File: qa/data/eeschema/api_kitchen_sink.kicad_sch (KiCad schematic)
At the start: 1 part

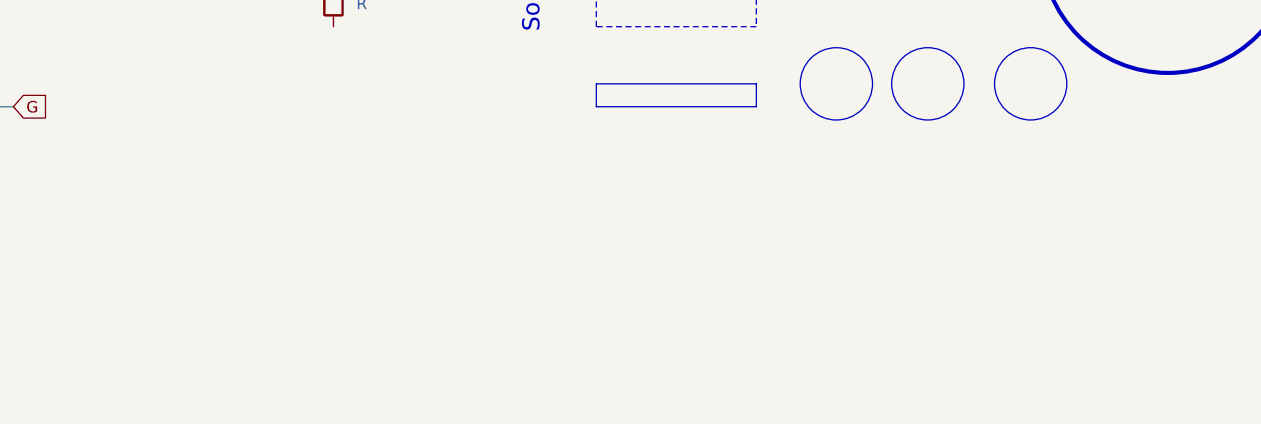
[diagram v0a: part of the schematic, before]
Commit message: API: add sch group and sheet symbol support
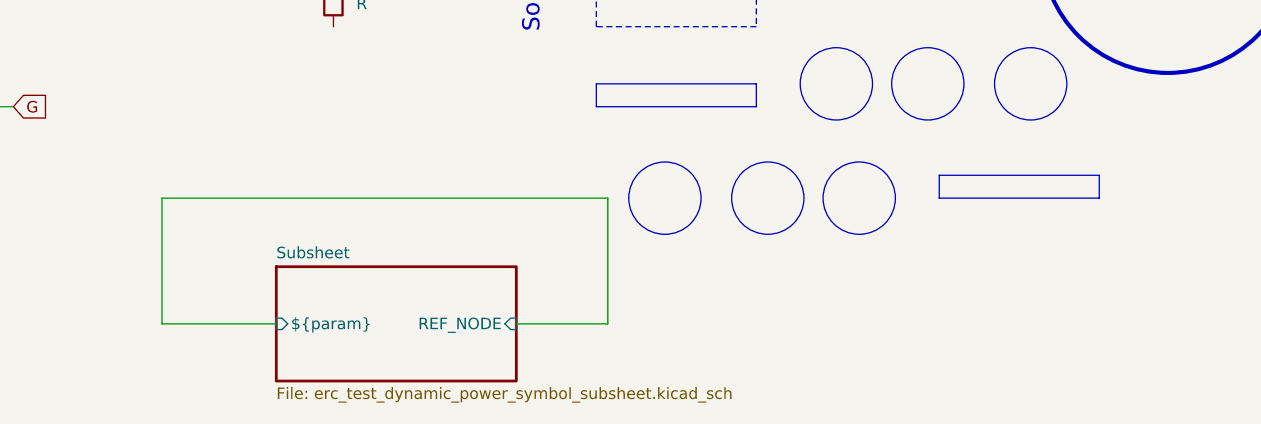
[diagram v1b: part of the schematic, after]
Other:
- added sheet Subsheet (erc_test_dynamic_power_symbol_subsheet.kicad_sch)
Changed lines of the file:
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@@
 		)
+	)
+	(circle
+		(center 157.48 63.5)
+		(radius 4.0161)
+		(stroke
+			(width 0)
+			(type solid)
+		)
+		(fill
+			(type cross_hatch)
+			(color 58 104 255 1)
+		)
+		(locked yes)
 	)
 	(bezier
@@
 	)
 	(circle
+		(center 167.64 63.5)
+		(radius 4.0161)
+		(stroke
+			(width 0)
+			(type default)
+		)
+		(fill
+			(type none)
+		)
+		(locked yes)
+	)
+	(circle
 		(center 201.93 35.56)
 		(radius 14.0276)
@@
 			(type none)
 		)
+	)
+	(circle
+		(center 146.05 63.5)
+		(radius 4.0161)
+		(stroke
+			(width 0)
+			(type solid)
+		)
+		(fill
+			(type reverse_hatch)
+			(color 0 0 0 0)
+		)
+		(locked yes)
+	)
+	(rectangle
+		(start 194.31 63.5)
+		(end 176.53 60.96)
+		(stroke
+			(width 0)
+			(type solid)
+		)
+		(fill
+			(type hatch)
+			(color 255 64 87 1)
+		)
+		(locked yes)
 	)
 	(text "Some text"
@@
 	(wire
 		(pts
+			(xy 102.87 77.47) (xy 90.17 77.47)
+		)
+		(stroke
+			(width 0)
+			(type default)
+		)
+	)
+	(wire
+		(pts
 			(xy 59.69 40.64) (xy 59.69 53.34)
 		)
@@
 	(wire
 		(pts
+			(xy 139.7 77.47) (xy 129.54 77.47)
+		)
+		(stroke
+			(width 0)
+			(type default)
+		)
+	)
+	(wire
+		(pts
 			(xy 87.63 27.94) (xy 80.01 27.94)
 		)
@@
 		(pts
 			(xy 48.26 25.4) (xy 48.26 19.05)
+		)
+		(stroke
+			(width 0)
+			(type default)
+		)
+	)
+	(wire
+		(pts
+			(xy 90.17 77.47) (xy 90.17 63.5)
 		)
 		(stroke
@@
 	(wire
 		(pts
+			(xy 139.7 63.5) (xy 139.7 77.47)
+		)
+		(stroke
+			(width 0)
+			(type default)
+		)
+	)
+	(wire
+		(pts
 			(xy 53.34 40.64) (xy 59.69 40.64)
 		)
@@
 		(pts
 			(xy 59.69 40.64) (xy 80.01 40.64)
+		)
+		(stroke
+			(width 0)
+			(type default)
+		)
+	)
+	(wire
+		(pts
+			(xy 90.17 63.5) (xy 139.7 63.5)
 		)
 		(stroke
@@
 				)
 			)
+		)
+	)
+	(group "MyGroup"
+		(locked yes)
+		(members "1c20a5ba-7190-401a-b021-abb688d52ffd" "bf6e7e59-beed-4ba7-a7bf-ffa7476e6e5d"
+			"e335506b-7a34-4e1e-bd33-077d7ea2b1b5" "e3e9fe17-b56a-4c49-a669-9d6f9adbbbc8"
+		)
+	)
+	(sheet
+		(at 102.87 71.12)
+		(size 26.67 12.7)
+		(exclude_from_sim no)
+		(in_bom yes)
+		(on_board yes)
+		(dnp no)
+		(fields_autoplaced yes)
+		(stroke
+			(width 0.3048)
+			(type solid)
+			(color 139 160 255 1)
+		)
+		(fill
+			(color 247 255 168 0.3607843137)
+		)
+		(property "Sheetname" "Subsheet"
+			(at 102.87 70.3322 0)
+			(show_name no)
+			(do_not_autoplace no)
+			(effects
+				(font
+					(size 1.27 1.27)
+				)
+				(justify left bottom)
+			)
+		)
+		(property "Sheetfile" "erc_test_dynamic_power_symbol_subsheet.kicad_sch"
+			(at 102.87 84.4808 0)
+			(show_name no)
+			(do_not_autoplace no)
+			(effects
+				(font
+					(size 1.27 1.27)
+				)
+				(justify left top)
+			)
+		)
+		(property "param" "Test"
+			(at 102.87 71.12 0)
+			(hide yes)
+			(show_name no)
+			(do_not_autoplace no)
+			(effects
+				(font
+					(size 1.27 1.27)
+				)
+			)
+		)
+		(pin "${param}" input
+			(at 102.87 77.47 180)
+			(effects
+				(font
+					(size 1.27 1.27)
+				)
+				(justify left)
+			)
+		)
+		(pin "REF_NODE" input
+			(at 129.54 77.47 0)
+			(effects
+				(font
+					(size 1.27 1.27)
+				)
+				(justify right)
+			)
+		)
+		(instances
+			(project "api_kitchen_sink"
+				(path "/d6ee7e6a-6570-43fd-93e6-b98f9cea3e37"
+					(page "2")
+				)
+			)
